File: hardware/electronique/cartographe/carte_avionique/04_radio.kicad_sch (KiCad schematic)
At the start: 6 parts, among them J401 VERS MODULE RP4TD, J402 ADAPTATEUR UART PIXHAWK

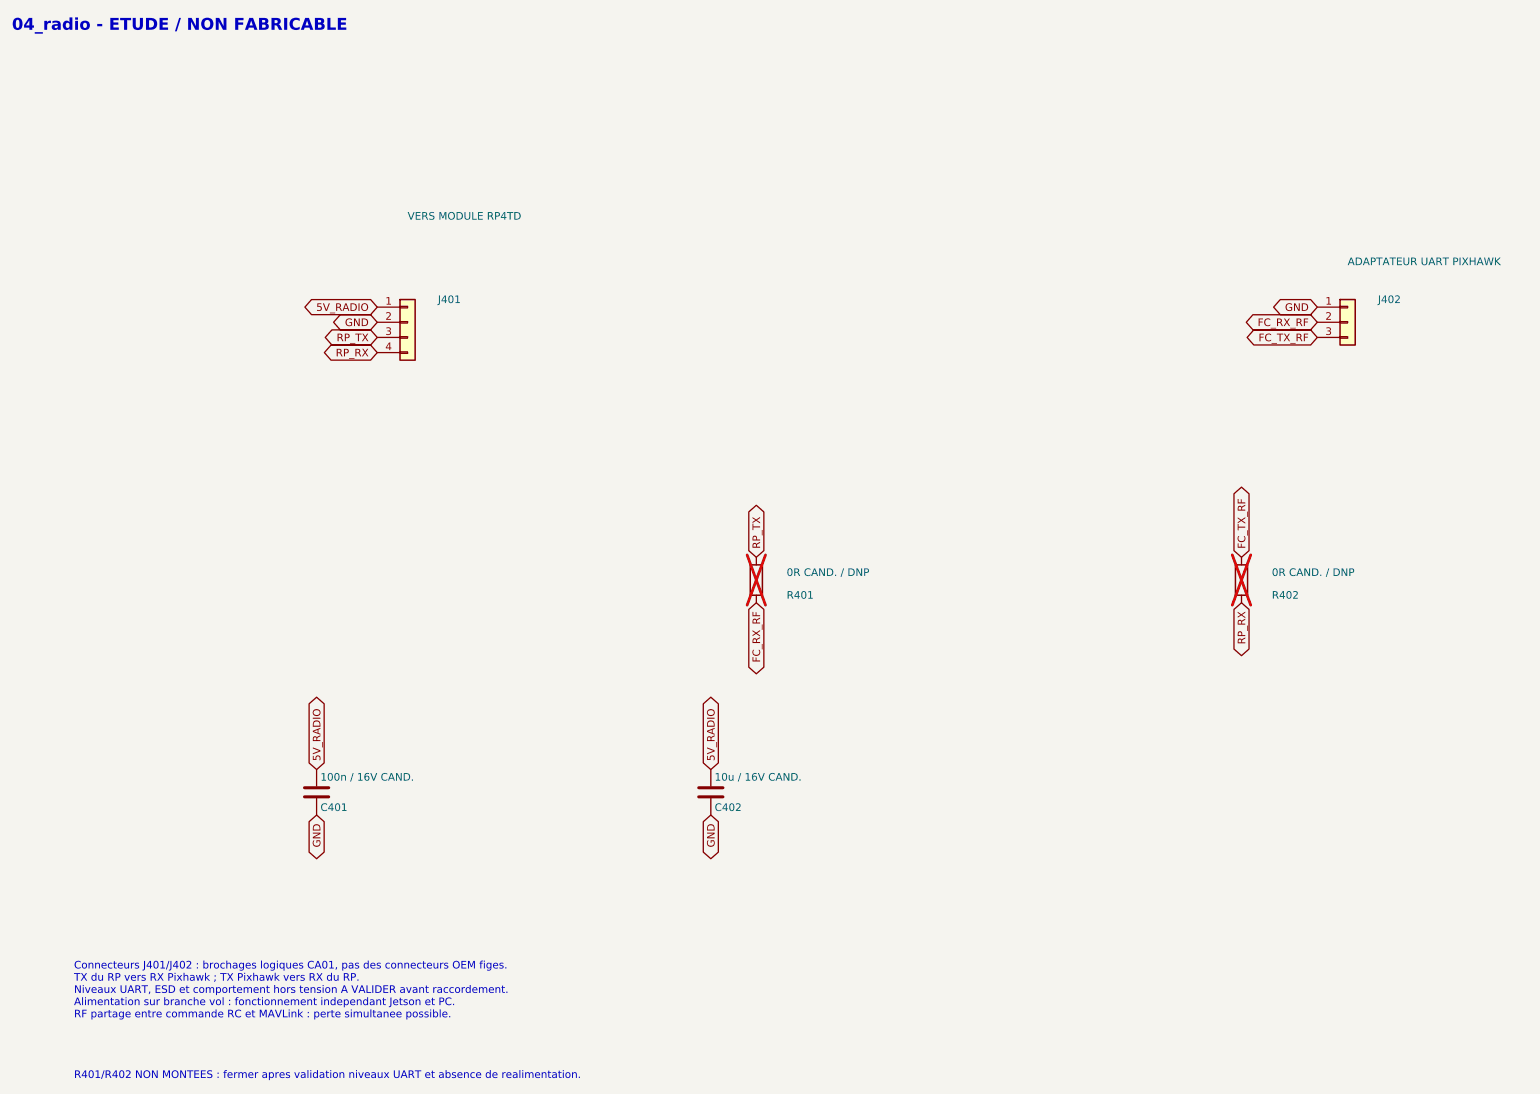
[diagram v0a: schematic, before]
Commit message: feat(hw): compléter CA01 et clarifier la synchronisation des captures
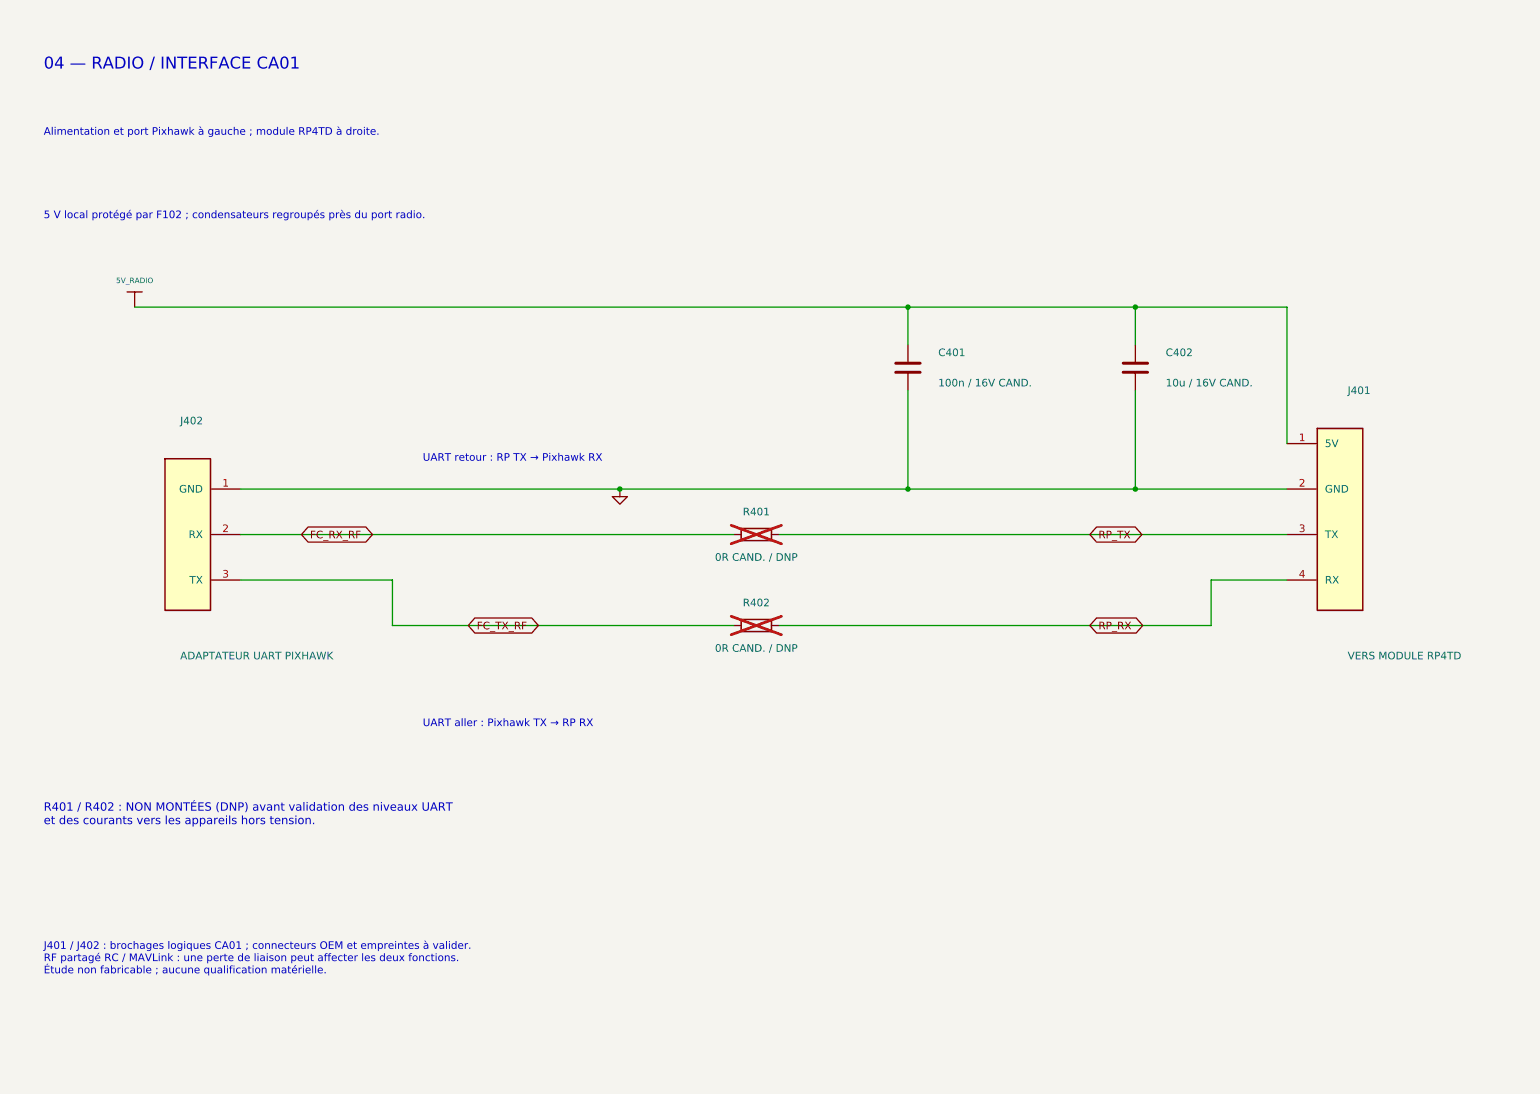
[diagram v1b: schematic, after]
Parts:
- J401: symbol Connector_Generic:Conn_01x04 -> CA01_Fonctions:Radio_RP4TD_R
- J402: symbol Connector_Generic:Conn_01x03 -> CA01_Fonctions:Radio_UART_Pixhawk_L
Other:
- note added: "04 — RADIO / INTERFACE CA01"
- note added: "5 V local protégé par F102 ; condensateurs regroupés près du port radio."
- note added: "Alimentation et port Pixhawk à gauche ; module RP4TD à droite."
- note added: "J401 / J402 : brochages logiques CA01 ; connecteurs OEM et empreintes à valider. RF partagé RC / MAVLink : une perte de liaison peut affecter les deux fonctions. Étude non fabricable ; aucune qualification matérielle."
- note added: "R401 / R402 : NON MONTÉES (DNP) avant validation des niveaux UART et des courants vers les appareils hors tension."
- note added: "UART aller : Pixhawk TX → RP RX"
- note added: "UART retour : RP TX → Pixhawk RX"
- note removed: "04_radio - ETUDE / NON FABRICABLE"
- note removed: "Connecteurs J401/J402 : brochages logiques CA01, pas des connecteurs OEM figes. TX du RP vers RX Pixhawk ; TX Pixhawk vers RX du RP. Niveaux UART, ESD et comportement hors tension A VALIDER avant raccordement. Alimentation sur branche vol : fonctionnement independant Jetson et PC. RF partage entre commande RC et MAVLink : perte simultanee possible."
- note removed: "R401/R402 NON MONTEES : fermer apres validation niveaux UART et absence de realimentation."
- moved on the sheet: C401, C402, J401, J402, R401, R402
